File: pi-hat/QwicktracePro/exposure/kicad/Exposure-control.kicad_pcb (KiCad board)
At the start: 2 copper layers, 50 x 35 mm, 10 parts, among them J1 Light Control, J2 Power, J3 HDMI, J4 Fan, J5 Safelight Control, J7 UVPanel, Q1 BD139, U1 AMZ_3A_MOD

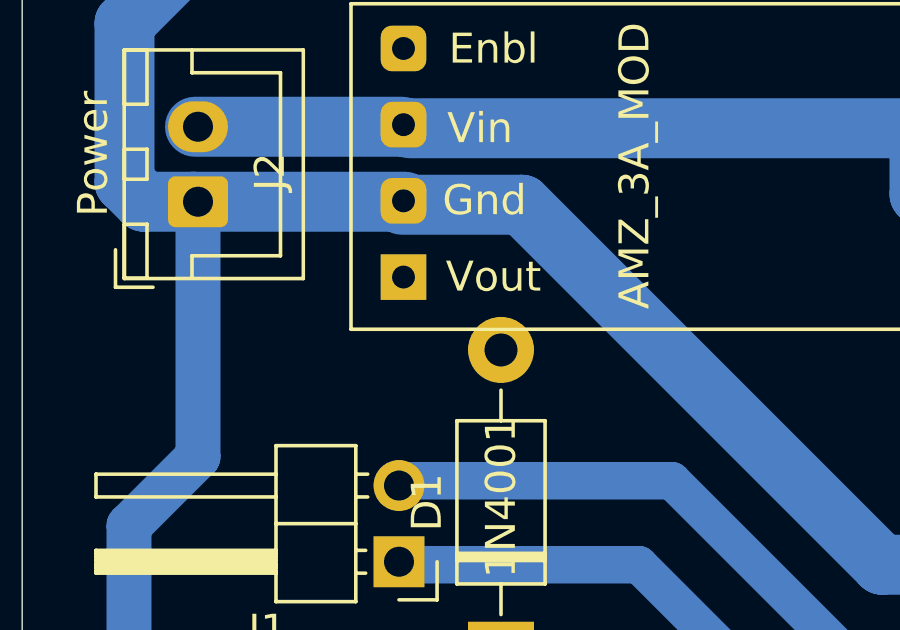
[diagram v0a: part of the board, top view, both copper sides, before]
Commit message: Fixes to exposure control board
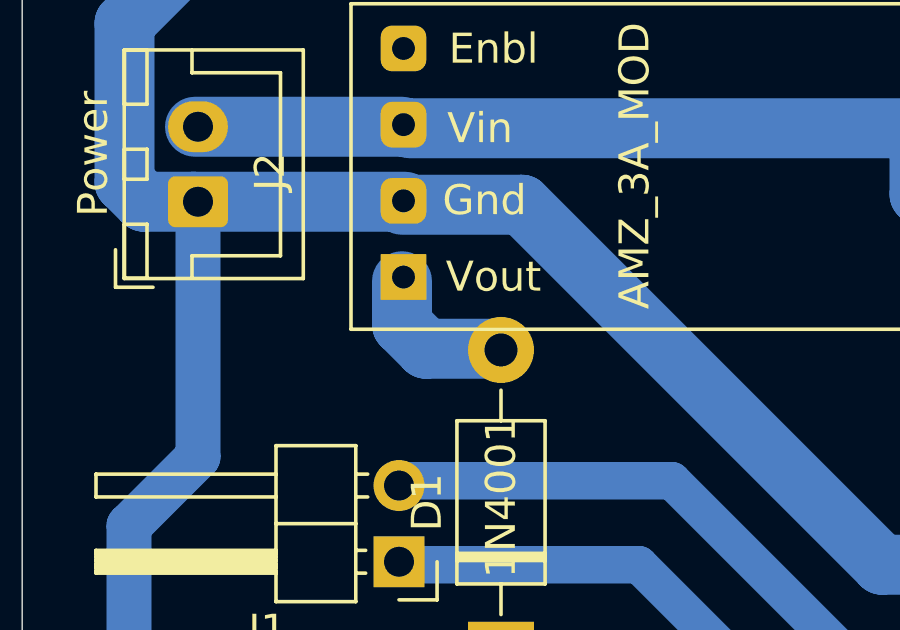
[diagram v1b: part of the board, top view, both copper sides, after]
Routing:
- net Net-(D1-Pad2): track 0.00 -> 4.98 mm

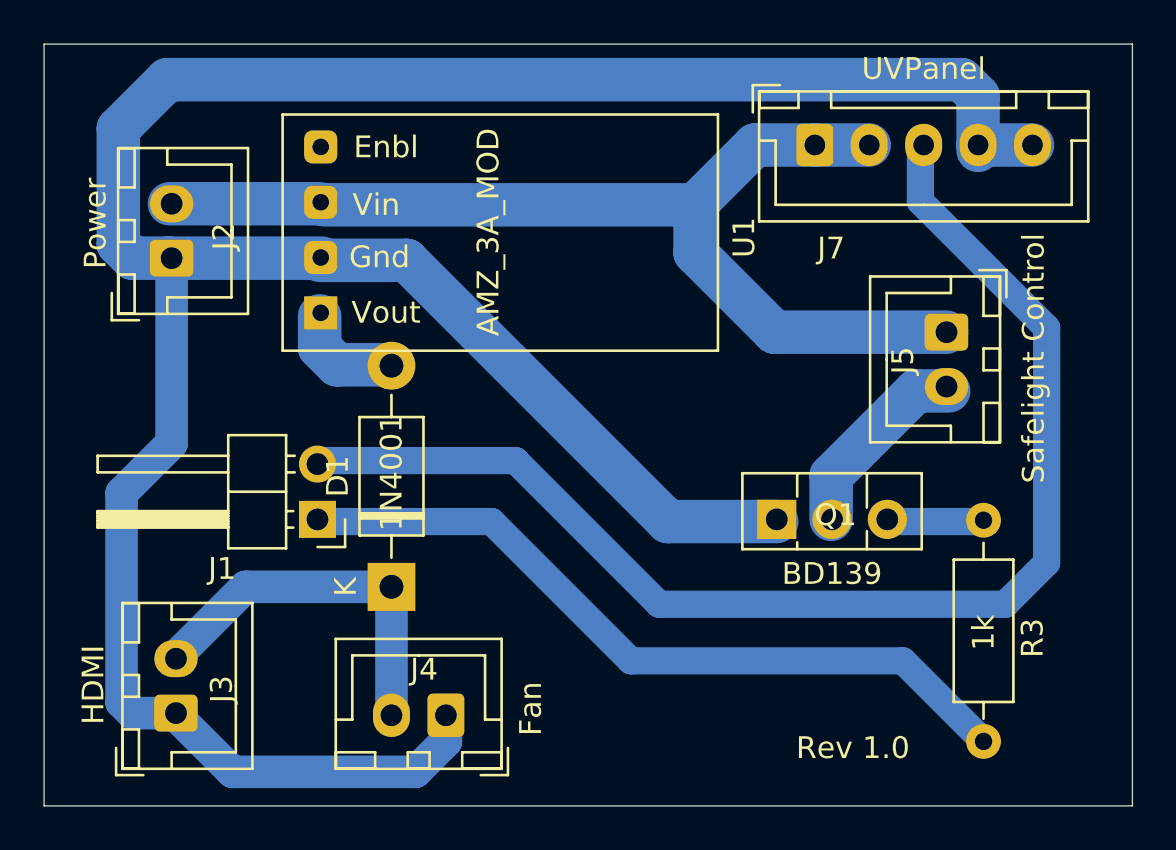
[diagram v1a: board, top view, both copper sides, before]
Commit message: Exposure control board rev 1.5
Moved signal connectors to opposite side.  Added screw hole to connect to exposure table body
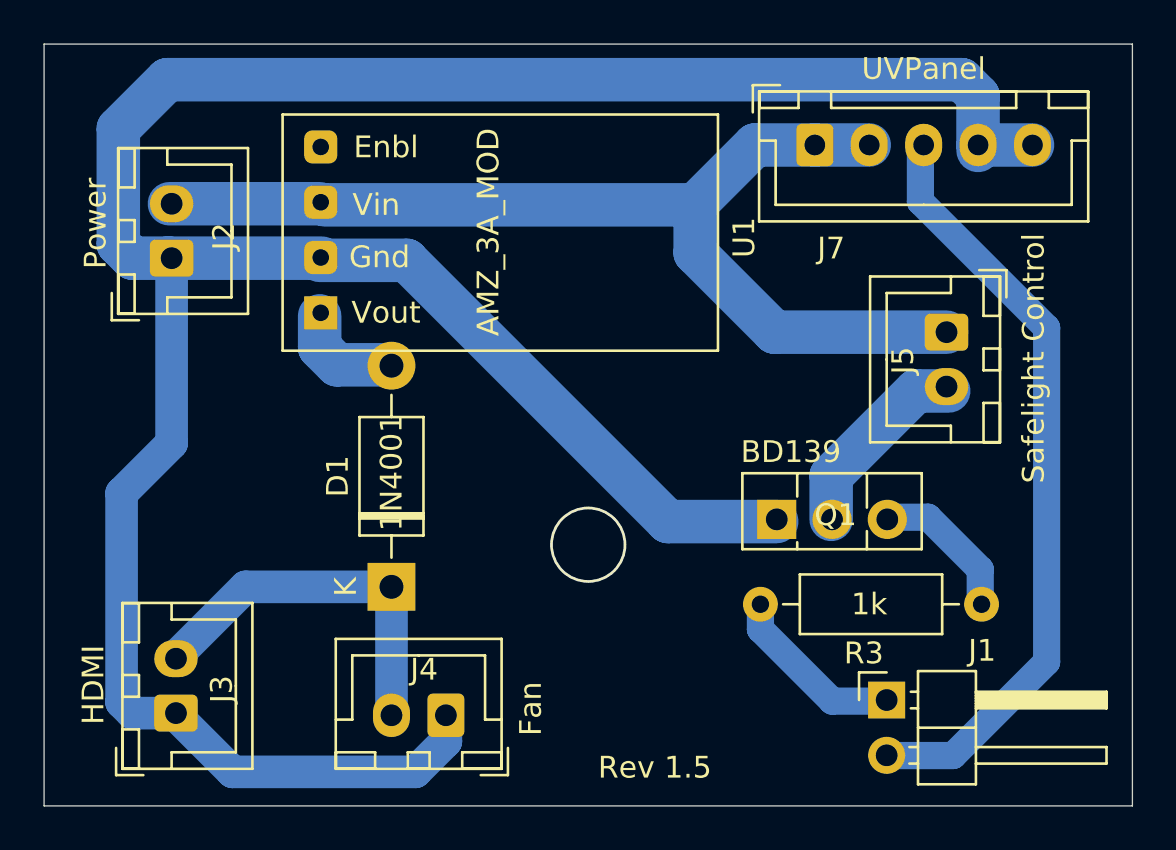
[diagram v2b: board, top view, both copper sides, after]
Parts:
- moved J1 27.4 mm to (48.7, 67.1), turned to 0 degrees
- moved R3 12.0 mm to (42.9, 62.7), turned to 0 degrees
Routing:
- net SafelightControl: track 34.7 -> 8.17 mm
- net UVControl: track 58.8 -> 35.7 mm
- net Net-(Q1-Pad3): track 4.20 -> 6.64 mm
- net (no net): vias 0 -> 1
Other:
- board text added: "Rev 1.5"
- board text removed: "Rev 1.0"
